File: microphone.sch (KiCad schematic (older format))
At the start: 8 parts, among them P1 BLC, P2 SB, P3 E, P4 PTT, P5 MIC-E, P6 MIC, P7 HK, P8 DM

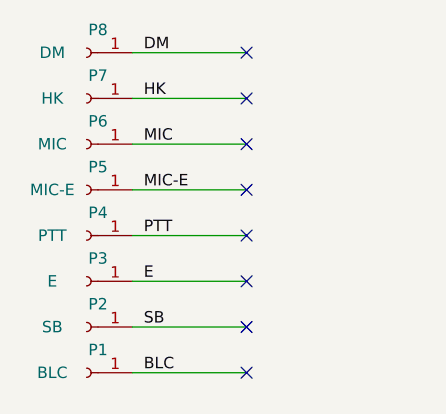
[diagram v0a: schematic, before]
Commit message: Adds wirepads.
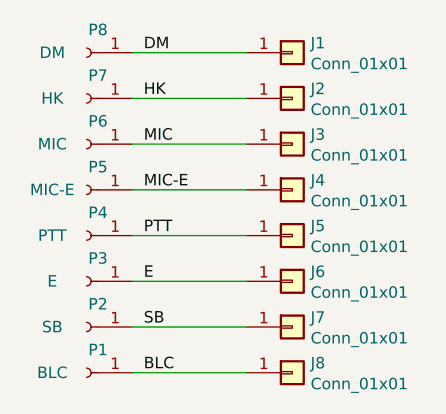
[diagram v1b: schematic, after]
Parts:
- added J1, J2, J3, J4, J5, J6, J7, J8: Conn_01x01, Connector_Wire:SolderWire-0.1sqmm_1x01_D0.4mm_OD1mm, symbol Connector_Generic:Conn_01x01
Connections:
- net BLC: now also J8.1 (Pin_1)
- net DM: now also J1.1 (Pin_1)
- net E: now also J6.1 (Pin_1)
- net HK: now also J2.1 (Pin_1)
- net MIC: now also J3.1 (Pin_1)
- net MIC-E: now also J4.1 (Pin_1)
- net PTT: now also J5.1 (Pin_1)
- net SB: now also J7.1 (Pin_1)
- no-connect marks 8 -> 0
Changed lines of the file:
@@
 	-1   0    0    1
 $EndComp
+Text Label 5200 4550 0    50   ~ 0
+BLC
+Text Label 5200 4350 0    50   ~ 0
+SB
+Text Label 5200 4150 0    50   ~ 0
+E
+Text Label 5200 3950 0    50   ~ 0
+PTT
+Text Label 5200 3750 0    50   ~ 0
+MIC-E
+Text Label 5200 3550 0    50   ~ 0
+MIC
+Text Label 5200 3350 0    50   ~ 0
+HK
+Text Label 5200 3150 0    50   ~ 0
+DM
 Wire Wire Line
 	5150 4550 5650 4550
@@
 Wire Wire Line
 	5150 3150 5650 3150
-NoConn ~ 5650 3150
-NoConn ~ 5650 3350
-NoConn ~ 5650 3550
-NoConn ~ 5650 3750
-NoConn ~ 5650 3950
-NoConn ~ 5650 4150
-NoConn ~ 5650 4350
-NoConn ~ 5650 4550
-Text Label 5200 4550 0    50   ~ 0
-BLC
-Text Label 5200 4350 0    50   ~ 0
-SB
-Text Label 5200 4150 0    50   ~ 0
-E
-Text Label 5200 3950 0    50   ~ 0
-PTT
-Text Label 5200 3750 0    50   ~ 0
-MIC-E
-Text Label 5200 3550 0    50   ~ 0
-MIC
-Text Label 5200 3350 0    50   ~ 0
-HK
-Text Label 5200 3150 0    50   ~ 0
-DM
+$Comp
+L Connector_Generic:Conn_01x01 J8
+U 1 1 60252E0D
+P 5850 4550
+F 0 "J8" H 5930 4592 50  0000 L CNN
+F 1 "Conn_01x01" H 5930 4501 50  0000 L CNN
+F 2 "Connector_Wire:SolderWire-0.1sqmm_1x01_D0.4mm_OD1mm" H 5850 4550 50  0001 C CNN
+F 3 "~" H 5850 4550 50  0001 C CNN
+	1    5850 4550
+	1    0    0    -1
+$EndComp
+$Comp
+L Connector_Generic:Conn_01x01 J7
+U 1 1 602528DD
+P 5850 4350
+F 0 "J7" H 5930 4392 50  0000 L CNN
+F 1 "Conn_01x01" H 5930 4301 50  0000 L CNN
+F 2 "Connector_Wire:SolderWire-0.1sqmm_1x01_D0.4mm_OD1mm" H 5850 4350 50  0001 C CNN
+F 3 "~" H 5850 4350 50  0001 C CNN
+	1    5850 4350
+	1    0    0    -1
+$EndComp
+$Comp
+L Connector_Generic:Conn_01x01 J6
+U 1 1 602521F7
+P 5850 4150
+F 0 "J6" H 5930 4192 50  0000 L CNN
+F 1 "Conn_01x01" H 5930 4101 50  0000 L CNN
+F 2 "Connector_Wire:SolderWire-0.1sqmm_1x01_D0.4mm_OD1mm" H 5850 4150 50  0001 C CNN
+F 3 "~" H 5850 4150 50  0001 C CNN
+	1    5850 4150
+	1    0    0    -1
+$EndComp
+$Comp
+L Connector_Generic:Conn_01x01 J5
+U 1 1 60251BD7
+P 5850 3950
+F 0 "J5" H 5930 3992 50  0000 L CNN
+F 1 "Conn_01x01" H 5930 3901 50  0000 L CNN
+F 2 "Connector_Wire:SolderWire-0.1sqmm_1x01_D0.4mm_OD1mm" H 5850 3950 50  0001 C CNN
+F 3 "~" H 5850 3950 50  0001 C CNN
+	1    5850 3950
+	1    0    0    -1
+$EndComp
+$Comp
+L Connector_Generic:Conn_01x01 J4
+U 1 1 602516BF
+P 5850 3750
+F 0 "J4" H 5930 3792 50  0000 L CNN
+F 1 "Conn_01x01" H 5930 3701 50  0000 L CNN
+F 2 "Connector_Wire:SolderWire-0.1sqmm_1x01_D0.4mm_OD1mm" H 5850 3750 50  0001 C CNN
+F 3 "~" H 5850 3750 50  0001 C CNN
+	1    5850 3750
+	1    0    0    -1
+$EndComp
+$Comp
+L Connector_Generic:Conn_01x01 J3
+U 1 1 60251245
+P 5850 3550
+F 0 "J3" H 5930 3592 50  0000 L CNN
+F 1 "Conn_01x01" H 5930 3501 50  0000 L CNN
+F 2 "Connector_Wire:SolderWire-0.1sqmm_1x01_D0.4mm_OD1mm" H 5850 3550 50  0001 C CNN
+F 3 "~" H 5850 3550 50  0001 C CNN
+	1    5850 3550
+	1    0    0    -1
+$EndComp
+$Comp
+L Connector_Generic:Conn_01x01 J2
+U 1 1 60250DB8
+P 5850 3350
+F 0 "J2" H 5930 3392 50  0000 L CNN
+F 1 "Conn_01x01" H 5930 3301 50  0000 L CNN
+F 2 "Connector_Wire:SolderWire-0.1sqmm_1x01_D0.4mm_OD1mm" H 5850 3350 50  0001 C CNN
+F 3 "~" H 5850 3350 50  0001 C CNN
+	1    5850 3350
+	1    0    0    -1
+$EndComp
+$Comp
+L Connector_Generic:Conn_01x01 J1
+U 1 1 6024D577
+P 5850 3150
+F 0 "J1" H 5930 3192 50  0000 L CNN
+F 1 "Conn_01x01" H 5930 3101 50  0000 L CNN
+F 2 "Connector_Wire:SolderWire-0.1sqmm_1x01_D0.4mm_OD1mm" H 5850 3150 50  0001 C CNN
+F 3 "~" H 5850 3150 50  0001 C CNN
+	1    5850 3150
+	1    0    0    -1
+$EndComp
 $EndSCHEMATC
